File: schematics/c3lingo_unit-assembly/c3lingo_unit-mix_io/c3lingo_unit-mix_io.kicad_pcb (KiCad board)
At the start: 2 copper layers, 100 x 50 mm, 42 parts, among them J201 Stage Line-In, J202 Mix Line-Out, J203 PowerSupply, J204 Inputs, J205 Output, U201 LM833N, U202 DRV134PA, U203 LM833N

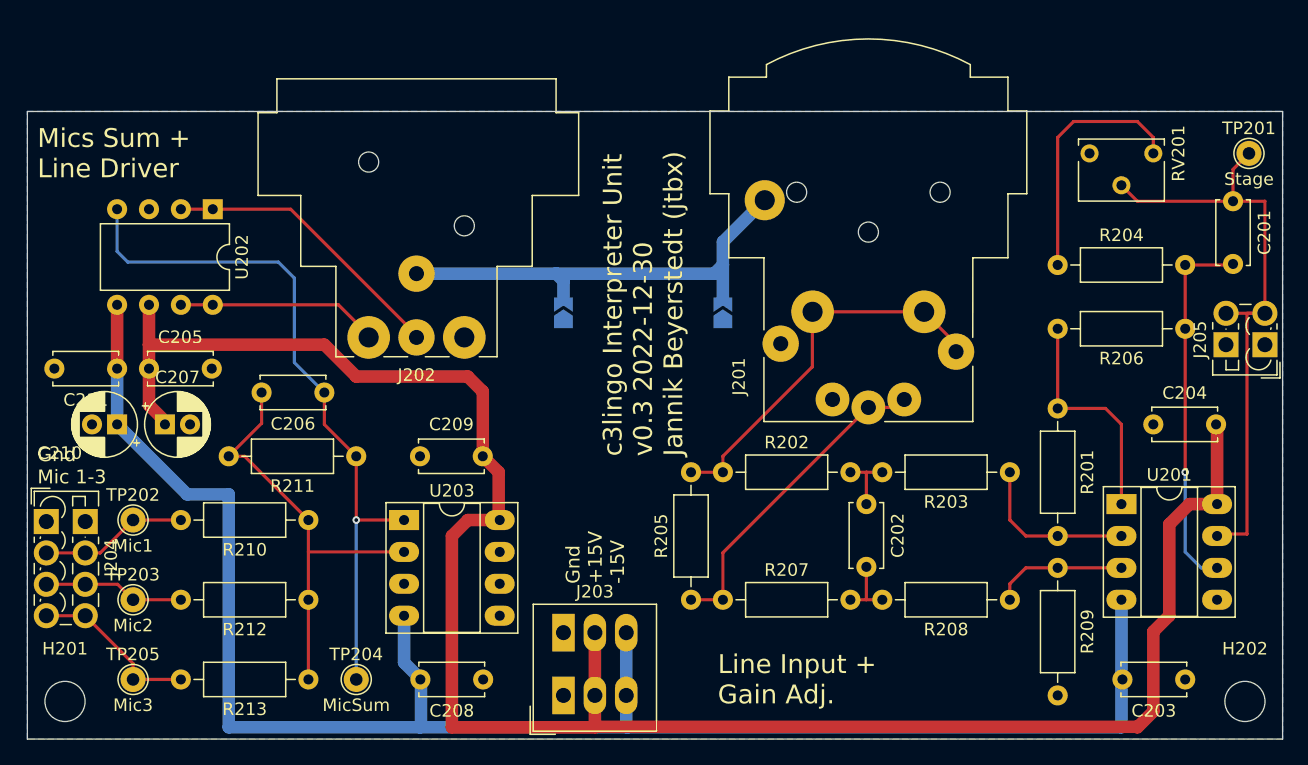
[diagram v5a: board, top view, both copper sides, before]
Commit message: Re-layout boards with SMD components
* Channel Mix: Removed vu meter potentiometer as good setting was found (10 dB
  more headroom)
* Channel Mix: Add vu meter alternate power
* Channel I/O: Added jumper for phantom power enable/disable
* Add GND test points
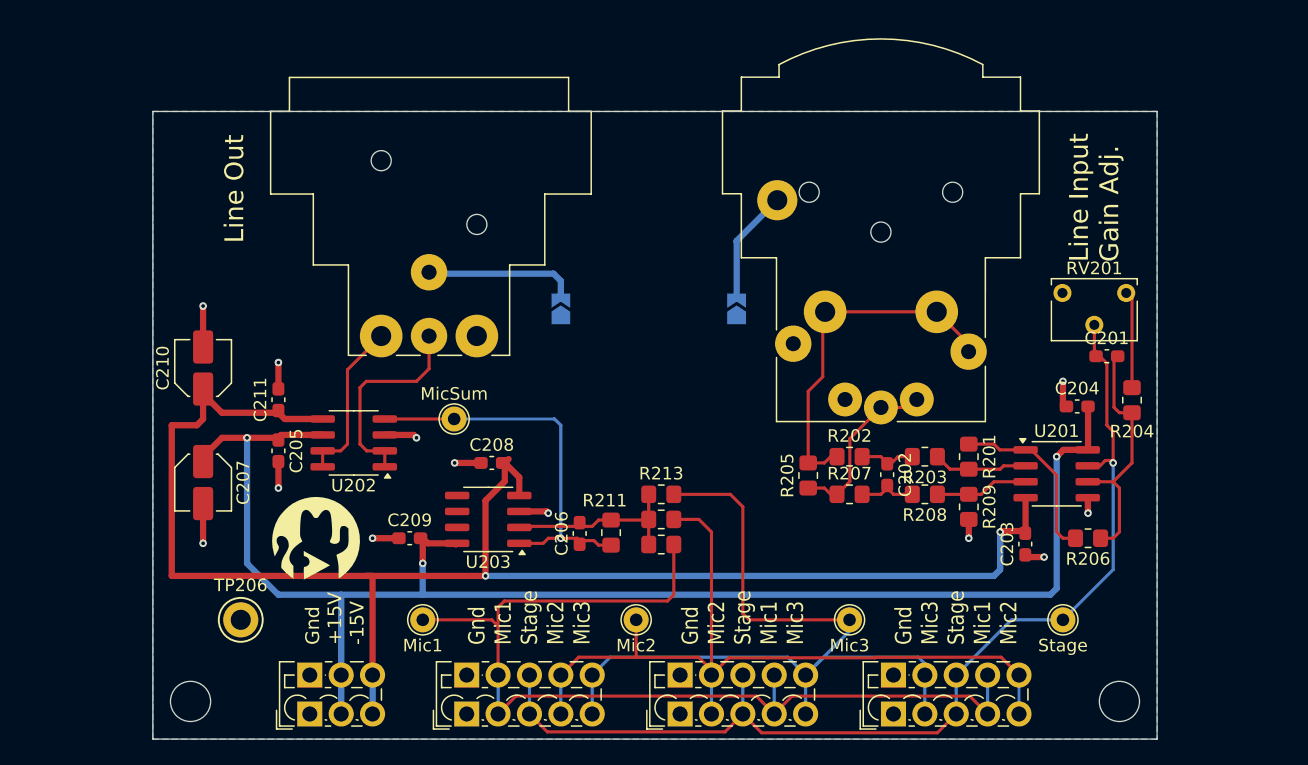
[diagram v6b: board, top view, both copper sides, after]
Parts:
- added G***: LOGO, c3lingo_unit-footprints:voctocat-07mm, F.Cu at (73.0, 84.0)
- added G***: LOGO, c3lingo_unit-footprints:voctocat-25mm, B.Cu at (100.0, 78.5)
- added J206: Ch3, TerminalBlock_Phoenix:TerminalBlock_Phoenix_PTSM-0,5-5-2.5-V-THR_1x05_P2.50mm_Vertical, F.Cu at (119.0, 98.0)
- added TP206: GND, TestPoint:TestPoint_Keystone_5005-5009_Compact, F.Cu at (67.0, 90.5)
- C201, C202, C203, C204, C205, C206, C208, C209, C211: footprint Capacitor_THT:C_Disc_D5.0mm_W2.5mm_P5.00mm -> Capacitor_SMD:C_0603_1608Metric_Pad1.08x0.95mm_HandSolder
- C207, C210: footprint Capacitor_THT:CP_Radial_D5.0mm_P2.00mm -> Capacitor_SMD:C_Elec_4x5.4
- J203: footprint TerminalBlock_Phoenix:TerminalBlock_Phoenix_PTSM-0,5-3-2.5-H-THR_1x03_P2.50mm_Horizontal -> TerminalBlock_Phoenix:TerminalBlock_Phoenix_PTSM-0,5-3-2.5-V-THR_1x03_P2.50mm_Vertical
- J204: value Inputs -> Ch1; footprint TerminalBlock_Phoenix:TerminalBlock_Phoenix_PTSM-0,5-4-2.5-V-THR_1x04_P2.50mm_Vertical -> TerminalBlock_Phoenix:TerminalBlock_Phoenix_PTSM-0,5-5-2.5-V-THR_1x05_P2.50mm_Vertical
- J205: value Output -> Ch2; footprint TerminalBlock_Phoenix:TerminalBlock_Phoenix_PTSM-0,5-2-2.5-V-THR_1x02_P2.50mm_Vertical -> TerminalBlock_Phoenix:TerminalBlock_Phoenix_PTSM-0,5-5-2.5-V-THR_1x05_P2.50mm_Vertical
- R201, R202, R203, R204, R205, R206, R207, R208, R209, R210, R211, R212, R213: footprint Resistor_THT:R_Axial_DIN0207_L6.3mm_D2.5mm_P10.16mm_Horizontal -> Resistor_SMD:R_0805_2012Metric_Pad1.20x1.40mm_HandSolder
- U201, U203: value LM833N -> LM833-N; footprint Package_DIP:DIP-8_W7.62mm_Socket_LongPads -> Package_SO:SOIC-8_3.9x4.9mm_P1.27mm
- U202: value DRV134PA -> DRV135UA; footprint Package_DIP:DIP-8_W7.62mm -> Package_SO:SOIC-8_3.9x4.9mm_P1.27mm
- moved TP205 57.3 mm to (115.5, 90.5)
- moved J205 55.1 mm to (102.0, 98.0), turned to 0 degrees
- moved TP203 40.1 mm to (98.5, 90.5)
- moved TP201 40.0 mm to (132.5, 90.5)
- moved J204 36.8 mm to (85.0, 98.0), turned to 0 degrees
- moved R213 31.7 mm to (100.5, 80.5), turned to 0 degrees
- moved R212 28.8 mm to (100.5, 82.5), turned to 0 degrees
- moved R210 28.2 mm to (100.5, 84.5), turned to 0 degrees
- moved TP202 24.4 mm to (81.5, 90.5)
- moved C206 23.2 mm to (94.0, 83.6), turned to 90 degrees
- moved TP204 22.2 mm to (84.0, 74.5)
- moved U202 21.7 mm to (76.0, 76.4), turned to 180 degrees
- moved R211 21.2 mm to (96.5, 83.5), turned to 90 degrees
- moved J203 20.3 mm to (72.5, 98.0)
- moved R206 18.4 mm to (134.5, 84.0)
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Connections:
- J204 pad 3: /Mic_Ch2 -> /StageSignal
- J204 pad 4: /Mic_Ch3 -> /Mic_Ch2
- J205 pad 2: /StageSignal -> /Mic_Ch2
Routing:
- net /Mic_Ch1: track 11.8 -> 81.1 mm
- net /Mic_Ch2: track 11.2 -> 65.8 mm
- net /Mic_Ch3: track 13.6 -> 67.7 mm
- net +15V: track 159.0 -> 119.2 mm, vias 0 -> 3
- net /StageSignal: track 49.8 -> 84.1 mm, vias 0 -> 1
- net Net-(U202-VIN): track 56.2 -> 31.1 mm
- net GND: track 0.00 -> 24.6 mm, vias 0 -> 12
- net Net-(U203A--): track 34.9 -> 15.5 mm
- net GNDREF: track 36.1 -> 22.3 mm
- net Net-(R204-Pad1): track 20.1 -> 7.73 mm
- net -15V: track 137.6 -> 125.6 mm, vias 0 -> 2
- net Net-(J201-Pad3): track 25.8 -> 14.0 mm
- net Net-(U201B--): track 29.8 -> 20.7 mm, vias 1 -> 0
- net Net-(U202-SENSE-): track 23.2 -> 16.7 mm
- net Net-(U201A--): track 13.2 -> 7.55 mm
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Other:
- board size 100 x 50 mm -> 80 x 50 mm
- board text added: "Gnd Mic1 Stage Mic2 Mic3"
- board text added: "Gnd Mic2 Stage Mic1 Mic3"
- board text added: "Gnd Mic3 Stage Mic1 Mic2"
- board text added: "Line Input Gain Adj."
- board text added: "Line Out"
- board text added: "c3lingo Interpreter Unit Mix I/O v0.3 2024-07-06"
- board text removed: "Gnd Mic 1-3"
- board text removed: "Line Input + Gain Adj."
- board text removed: "Mics Sum + Line Driver"
- board text removed: "c3lingo Interpreter Unit v0.3 2022-12-30 Jannik Beyerstedt (jtbx)"

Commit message: Fix date on PCB dimensions PDF
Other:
- board text added: "c3lingo Interpreter Unit Mix I/O v0.3 2024-07-07"
- board text removed: "c3lingo Interpreter Unit Mix I/O v0.3 2024-07-06"
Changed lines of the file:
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@@
 	(title_block
 		(title "c3lingo interpeter unit -- channel strip")
-		(date "2022-12-31")
+		(date "2024-07-07")
 		(rev "v0.3")
 		(company "Jannik Beyerstedt (jtbx)")
@@
 			)
 		)
-		(property "Model" "Vishay M64Y104"
+		(property "Model" "Bourns PV36Y104C01B00 or Vishay M64Y104"
 			(at 0 0 -90)
 			(unlocked yes)
@@
 		(layer "Edge.Cuts")
 	)
-	(gr_text "c3lingo Interpreter Unit\nMix I/O\nv0.3 2024-07-06"
+	(gr_text "c3lingo Interpreter Unit\nMix I/O\nv0.3 2024-07-07"
 		(at 100.5 57 0)
 		(layer "B.SilkS")

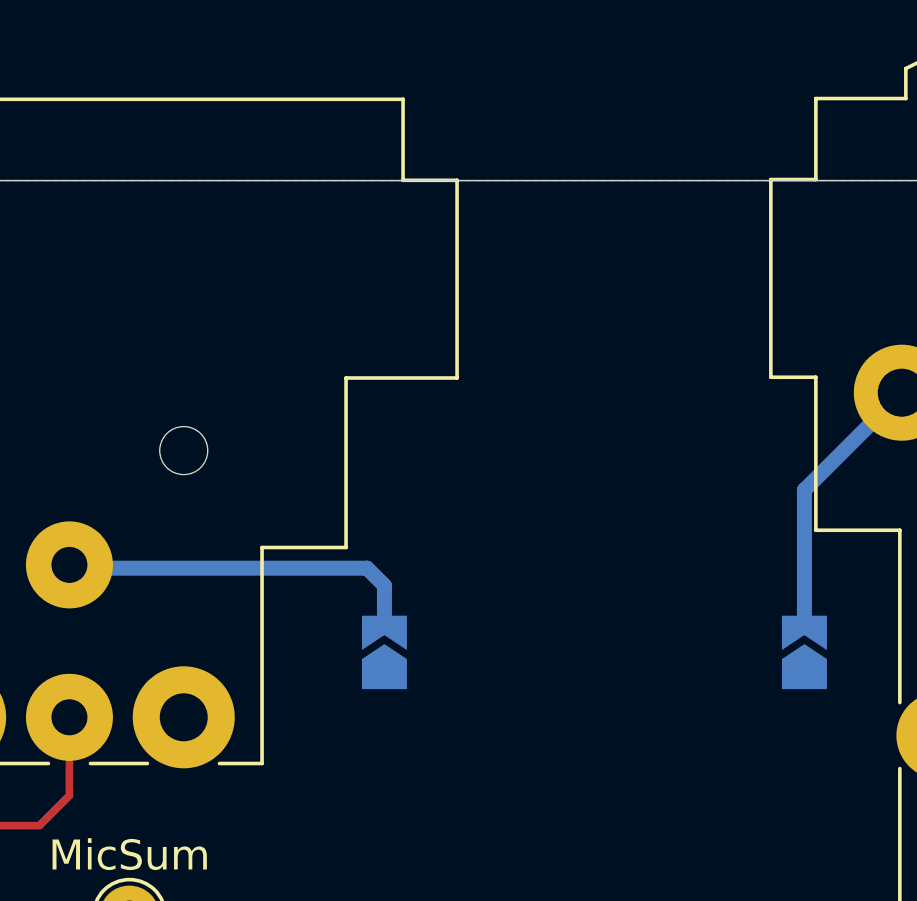
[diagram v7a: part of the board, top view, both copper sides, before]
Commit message: Mix I/O: Add ground lift
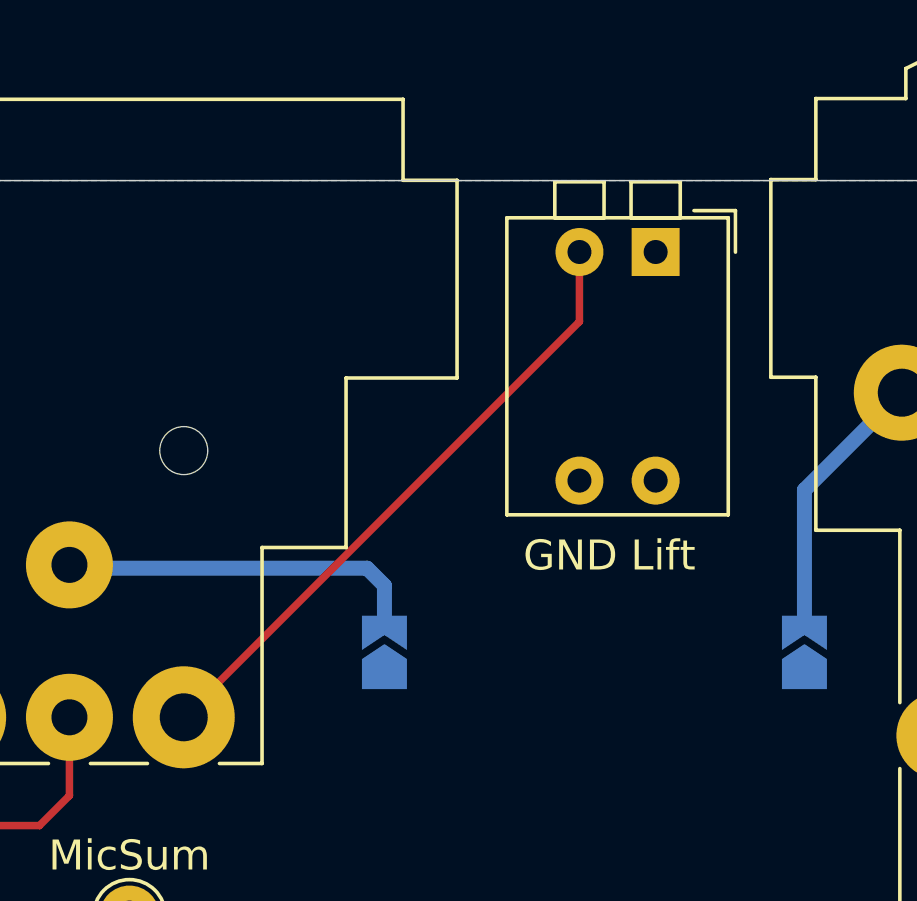
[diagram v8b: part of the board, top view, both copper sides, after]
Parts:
- added SW201: GND Lift, Button_Switch_THT:SW_DIP_SPSTx02_Piano_CTS_Series194-2MSTN_W7.62mm_P2.54mm, F.Cu at (101.5, 52.4)
- G***: footprint c3lingo_unit-footprints:voctocat-25mm -> c3lingo_unit-footprints:voctocat-15mm
- moved G*** 6.50 mm to (100.0, 72.0)
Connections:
- J202 pad 1: GND -> Net-(J202-Pad1)
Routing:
- net Net-(J202-Pad1): track 0.00 -> 21.0 mm
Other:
- board text added: "c3lingo Interpreter Unit Mix I/O v0.3.1 2024-07-08"
- board text removed: "c3lingo Interpreter Unit Mix I/O v0.3 2024-07-07"
